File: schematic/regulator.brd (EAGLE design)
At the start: 62 x 43 mm, 29 parts, among them J1 COMM, J2 STOP_LIGHT, J3 ON/OFF, J4 BATTERY, J5 DRIVER, J6 DRIVER POWER, Q1 NMOSFETSOT23, Q2 NMOSFETSOT23, Q3 NMOSFETSOT23, Q4 IRFR3607PBF

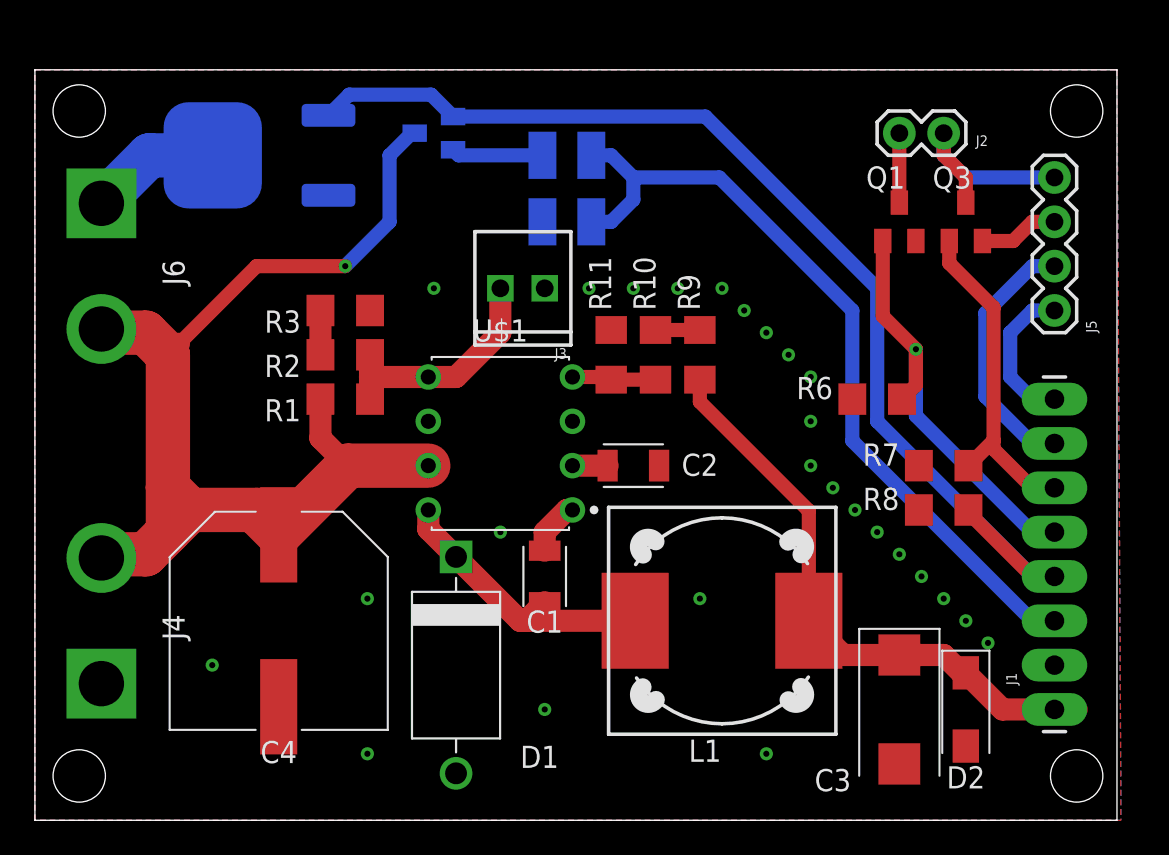
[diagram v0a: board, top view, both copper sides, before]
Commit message: Replace low-side BLDC driver switch by high-side switch
- Rearrange elements on regulator schematics
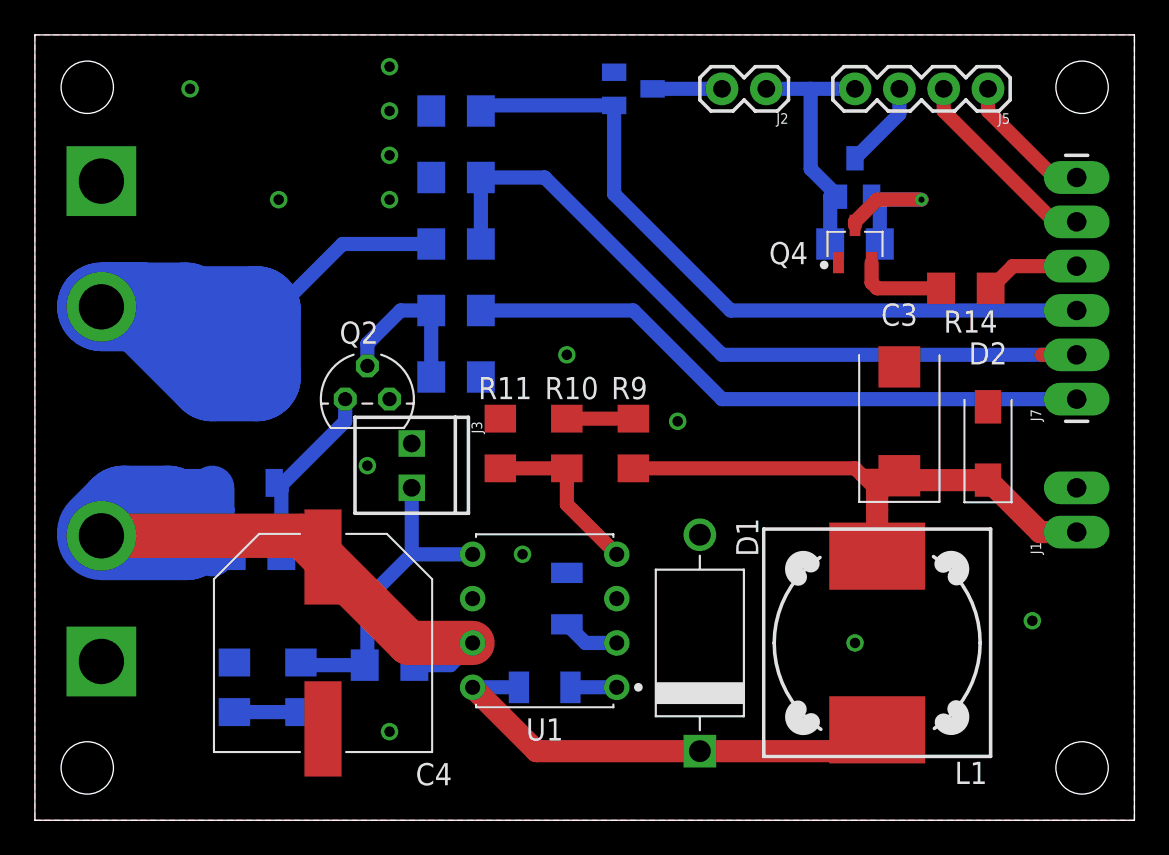
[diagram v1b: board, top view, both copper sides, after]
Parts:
- removed U$1: MAX5035PDIP8, eScooter:DIP826W56P254L937H458Q8B
- added J7: (no value), SparkFun-Connectors:1X06_LONGPADS
- added Q5: PMOSFET, Transistor:SOT23
- added R12, R13, R14: 10K, eagle-ltspice:R1206
- added U1: MAX5035PDIP8, eScooter:DIP826W56P254L937H458Q8B
- J1: value COMM -> (none); device SparkFun-Connectors:1X08_LONGPADS -> SparkFun-Connectors:1X02_LONGPADS
- Q2: value NMOSFETSOT23 -> NPN; device Transistor:SOT23 -> Transistor:TO92
- Q3: value NMOSFETSOT23 -> PMOSFET_TO252AA; device Transistor:SOT23 -> Transistor:D-PAK_TO252AA
- Q4: value IRFR3607PBF -> NPN; device Transistor:DPAK3 -> Transistor:SOT95P237X112-3N
- R4: value 1M -> 133K; device eagle-ltspice:R1210 -> eagle-ltspice:R1206
- R5: value 133K -> 1M; device eagle-ltspice:R1210 -> eagle-ltspice:R1206
- R7: value 10K -> 1K
- moved Q3 43.1 mm to (11.4, 24.1), flipped to the bottom
- moved R8 39.5 mm to (12.7, 15.2), flipped to the bottom, turned to 0 degrees
- moved Q4 34.7 mm to (47.0, 33.0), flipped to the top, turned to 90 degrees
- moved R6 29.2 mm to (24.1, 40.6), flipped to the bottom, turned to 0 degrees
- moved R3 22.5 mm to (11.4, 7.62), flipped to the bottom, turned to 270 degrees
- moved R2 19.2 mm to (15.2, 7.62), flipped to the bottom, turned to 270 degrees
- moved Q1 17.0 mm to (34.3, 41.9), flipped to the bottom, turned to 90 degrees
- moved C3 16.5 mm to (49.5, 22.9), turned to 90 degrees
- moved Q2 15.7 mm to (19.1, 24.1), flipped to the top, turned to 0 degrees
- moved R1 15.5 mm to (20.3, 8.89), flipped to the bottom
- moved D2 15.3 mm to (54.6, 21.6), turned to 90 degrees
- moved D1 14.0 mm to (38.1, 10.2), turned to 90 degrees
- moved R7 13.7 mm to (47.0, 33.0), flipped to the bottom, turned to 180 degrees
- moved J5 13.3 mm to (54.6, 41.9), turned to 180 degrees
- moved J3 11.7 mm to (21.6, 21.6), turned to 270 degrees
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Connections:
- removed net P$1: J6.GND, Q4.3
- new net N$10: Q2.2, R12.2, R13.2
- new net N$11: Q4.3, Q5.1, R7.2
- new net N$12: Q4.2, R14.2
- new net P$2: J6.VCC, Q3.4, R5.2
- net 5V: now also Q5.2, R7.1; no longer Q3.3
- net BAT: now also J7.2, R4.2, R5.1; no longer J1.3, R4.1, R5.2
- net GND: now also J6.GND, Q2.1, Q4.1, R13.1, R4.1, U1.3, U1.6; no longer Q4.2, R5.1, R7.1, R8.2, U$1.3, U$1.6
- net N$1: now also U1.1; no longer U$1.1
- net N$2: now also U1.8; no longer U$1.8
- net N$4: now also U1.2; no longer U$1.2
- net N$5: now also U1.5; no longer U$1.5
- net N$8: now also Q2.3, Q3.1, R8.1; no longer Q2.2, R4.2
- net N$9: now also U1.4; no longer U$1.4
- net PWM: now also J7.1, R12.1; no longer J1.4, Q2.1, Q4.1, R8.1
- net SPIN: now also J7.6; no longer J1.8
- net SPOUT: now also J7.5; no longer J1.7
- net ST: now also Q5.3; no longer Q3.2
- net STLEDCTL: now also J7.3; no longer J1.5
- net STOUT: now also J7.4, R14.1; no longer J1.6, Q3.1, R7.2
- net VIN: now also Q3.3, R8.2, U1.7; no longer J6.VCC, Q2.3, U$1.7
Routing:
- net P$2: track 0.00 -> 43.5 mm
- net PWM: track 64.6 -> 37.5 mm
- net STLEDCTL: track 24.7 -> 42.1 mm, vias 1 -> 0
- net STOUT: track 19.4 -> 5.45 mm
- net N$2: track 16.6 -> 27.9 mm
- net N$11: track 0.00 -> 10.4 mm, vias 0 -> 1
- net N$10: track 0.00 -> 9.53 mm
- net P$1: track 8.76 -> 0.00 mm
- net N$8: track 5.25 -> 11.6 mm
- net N$12: track 0.00 -> 5.27 mm
- net N$9: track 4.82 -> 10.1 mm
- net N$5: track 13.6 -> 18.6 mm
- net VIN: track 65.9 -> 62.4 mm, vias 1 -> 0
- net SPOUT: track 14.9 -> 11.5 mm
- net 5V: track 12.7 -> 15.1 mm
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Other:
- board size 62 x 43 mm -> 63 x 45 mm
- board text added: "12V"
- board text added: "5V"
- board text added: "BAT"
- board text added: "BATTERY"
- board text added: "DRIVER"
- board text added: "GND"
- board text added: "PWM"
- board text added: "SPIN"
- board text added: "SPOUT"
- board text added: "ST"
- board text added: "STGND"
- board text added: "STLED"
- board text added: "STOUT"

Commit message: Rework ECU board
- Align sizes
- Align elements placement on layers
- Change power traces in regulator
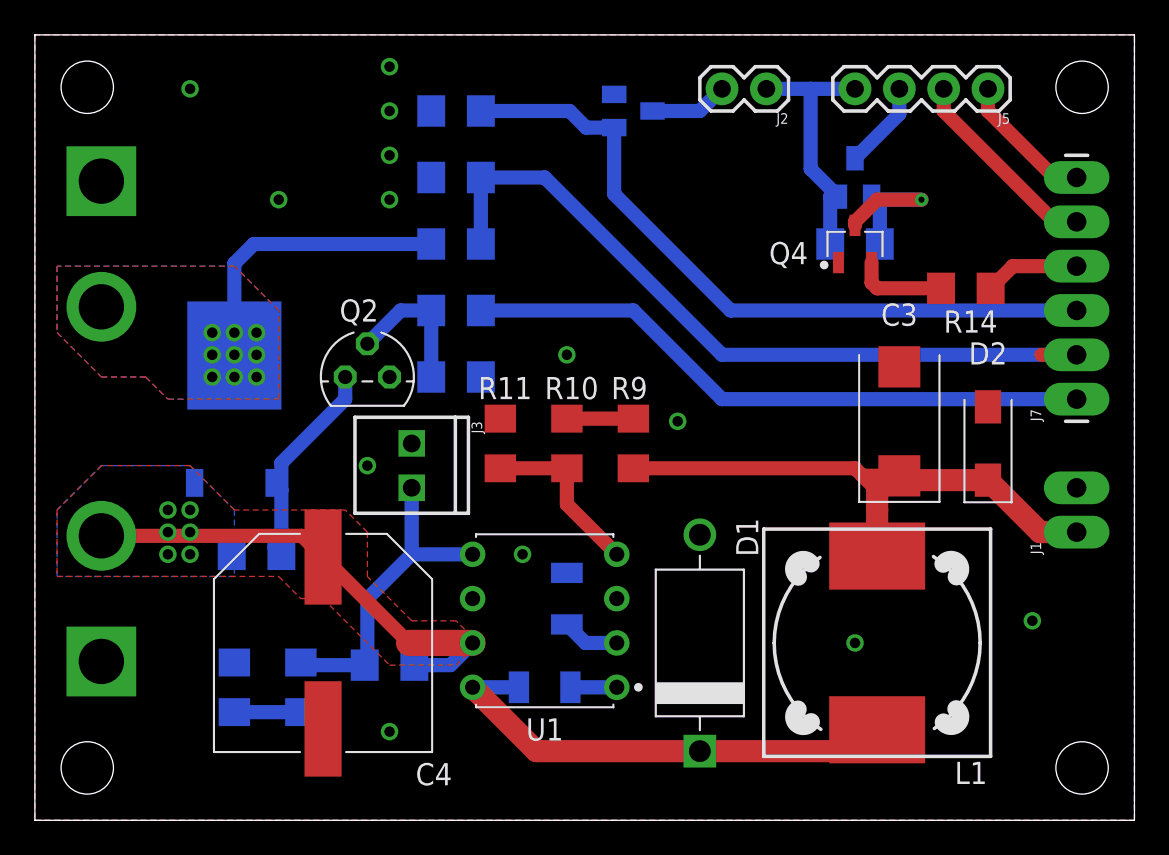
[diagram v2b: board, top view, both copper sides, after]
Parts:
- moved Q2 1.27 mm to (19.1, 25.4)
- moved Q1 1.27 mm to (34.3, 40.6)
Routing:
- net VIN: track 62.4 -> 27.7 mm, vias 0 -> 6
- net P$2: track 43.5 -> 17.0 mm, vias 0 -> 9
- net N$8: track 11.6 -> 12.8 mm
- net N$10: track 9.53 -> 8.26 mm
- net STLEDCTL: track 42.1 -> 41.1 mm
- net N$3: track 3.98 -> 4.51 mm
- added copper zone on layer 1, net P$2
- added copper zone on layer 16, net P$2
- added copper zone on layer 1, net VIN
- added copper zone on layer 16, net VIN

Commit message: Remove high-side switch for driver
- Keep driver alway on for now
- Add mosfet switched for speed and throttle
- Align break work
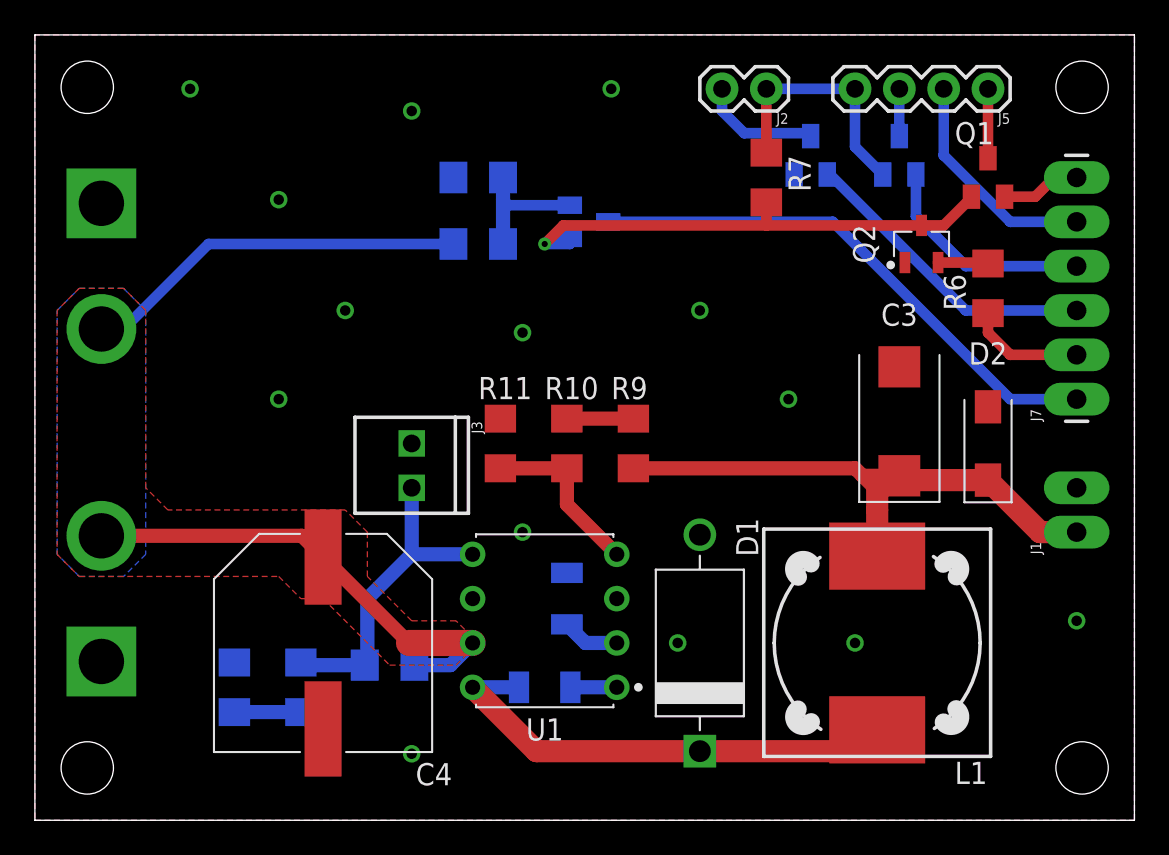
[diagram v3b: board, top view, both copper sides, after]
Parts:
- removed Q5: PMOSFET, Transistor:SOT23
- removed R12, R13, R14, R8: 10K, eagle-ltspice:R1206
- added Q7: NMOSFET, Transistor:SOT23
- Q1: value NMOSFETSOT23 -> PMOSFET
- Q2: device Transistor:TO92 -> Transistor:SOT95P237X112-3N
- Q3: value PMOSFET_TO252AA -> PMOSFET; device Transistor:D-PAK_TO252AA -> Transistor:SOT23
- Q4: value NPN -> PMOSFET; device Transistor:SOT95P237X112-3N -> Transistor:SOT23
- R7: value 1K -> 10K
- moved Q3 40.6 mm to (49.5, 38.1)
- moved Q2 32.7 mm to (50.8, 33.0), turned to 90 degrees
- moved R6 32.1 mm to (54.6, 30.5), flipped to the top, turned to 90 degrees
- moved Q1 20.7 mm to (54.6, 36.8), flipped to the top, turned to 0 degrees
- moved Q4 15.3 mm to (31.8, 34.3), flipped to the bottom
- moved R7 6.35 mm to (41.9, 36.8), flipped to the top, turned to 270 degrees
- moved J6 1.27 mm to (3.81, 31.8)
- moved R4 1.27 mm to (25.4, 36.8)
- moved R5 1.27 mm to (25.4, 33.0)
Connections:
- net SPOUT renamed SPEED_DR
- removed net N$10: Q2.2, R12.2, R13.2
- removed net N$11: Q4.3, Q5.1, R7.2
- removed net N$12: Q4.2, R14.2
- removed net N$8: Q2.3, Q3.1, R8.1
- removed net P$2: J6.VCC, Q3.4, R5.2
- removed net PWM: J7.1, R12.1
- removed net SPIN: J5.1, J7.6
- removed net ST: J5.3, Q5.3
- removed net STOUT: J7.4, R14.1
- new net BATOUT: Q4.2, R4.2, R5.1
- new net PWON: J7.2, R6.1
- new net PWON_REV: Q1.1, Q2.3, Q4.1, R7.2
- new net STCTL: J7.4, Q3.1
- new net STLEDOUT: J2.2, Q7.3
- new net ST_DR: J5.3, Q3.3
- new net THCTL: J7.6, Q1.2
- new net TH_DR: J5.1, Q1.3
- net 5V: now also Q3.2; no longer Q5.2
- net BAT: now also J7.1, Q4.3; no longer J7.2, R4.2, R5.1
- net GND: now also Q7.2; no longer Q1.2, Q4.1, R13.1, R6.2
- net N$3: now also Q2.2, R6.2; no longer J2.2, Q1.3
- net STLEDCTL: now also Q7.1; no longer Q1.1, R6.1
- net VIN: now also J6.VCC, R5.2; no longer Q3.3, R8.2
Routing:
- net PWM: track 37.5 -> 0.00 mm
- net PWON_REV: track 0.00 -> 28.7 mm, vias 0 -> 1
- net STLEDCTL: track 41.1 -> 17.5 mm
- net VIN: track 27.7 -> 50.4 mm, vias 6 -> 0
- net P$2: track 17.0 -> 0.00 mm, vias 9 -> 0
- net BAT: track 44.2 -> 31.0 mm
- net N$8: track 12.8 -> 0.00 mm
- net STCTL: track 0.00 -> 12.8 mm
- net N$11: track 10.4 -> 0.00 mm, vias 1 -> 0
- net BATOUT: track 0.00 -> 9.04 mm
- net N$10: track 8.26 -> 0.00 mm
- net SPIN: track 7.93 -> 0.00 mm
- net STLEDOUT: track 0.00 -> 6.95 mm
- net PWON: track 0.00 -> 6.72 mm
- net STOUT: track 5.45 -> 0.00 mm
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- removed copper zone on layer 1, net P$2
- removed copper zone on layer 16, net P$2
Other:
- board text added: "PWON"
- board text added: "SPEED"
- board text added: "TH"
- board text added: "THCTL"
- board text removed: "PWM"
- board text removed: "SPIN"
- board text removed: "SPOUT"
- board text removed: "STOUT"
